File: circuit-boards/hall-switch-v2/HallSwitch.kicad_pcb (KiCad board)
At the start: 2 copper layers, 19.1 x 17.8 mm, 16 parts, among them J1 0705550037, U1 US5881ESE

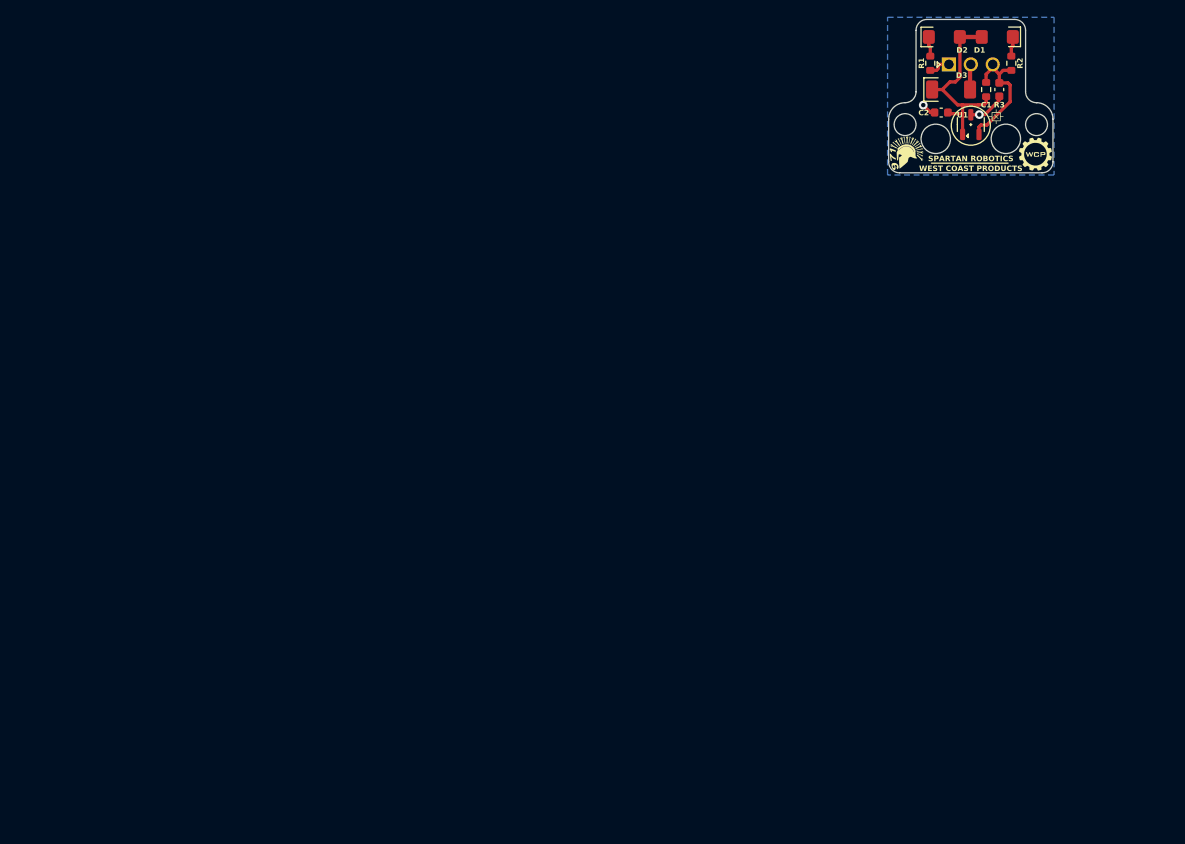
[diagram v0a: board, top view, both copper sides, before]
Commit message: Export files for new pcbs + board characteristics
Signed-off-by: Alex lenkov <Alexander.i.lenkov@gmail.com>
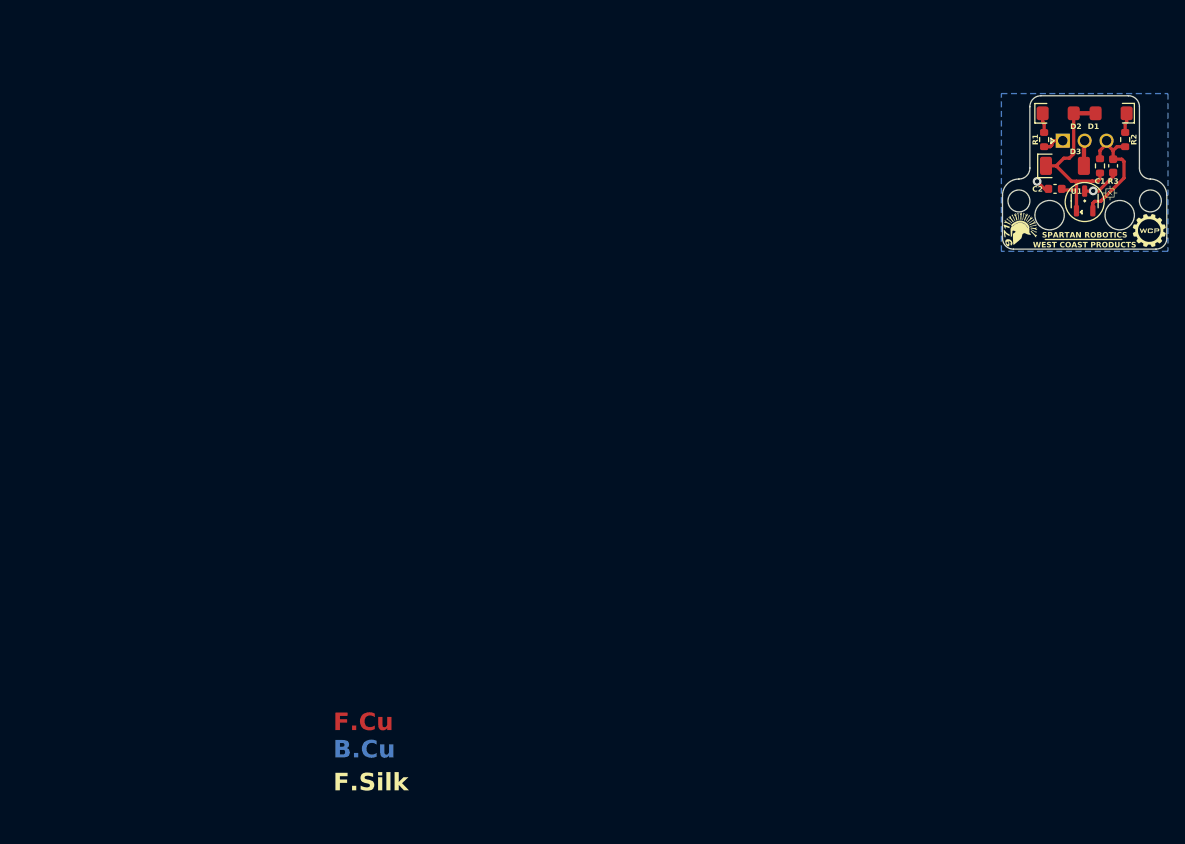
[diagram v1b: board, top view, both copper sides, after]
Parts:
- moved G*** 15.9 mm to (132.6, 115.2)
- moved G*** 15.9 mm to (140.2, 110.4)
- moved R1 15.9 mm to (135.5, 105.0)
- moved D1 15.9 mm to (143.3, 102.0)
- moved D2 15.9 mm to (137.2, 102.0)
- moved G*** 15.9 mm to (143.1, 111.2)
- moved G*** 15.9 mm to (147.7, 115.6)
- moved H1 15.9 mm to (132.6, 112.1)
- moved H2 15.9 mm to (147.8, 112.1)
- moved J1 15.9 mm to (140.2, 109.5)
- moved U1 15.9 mm to (140.2, 112.1)
- moved C1 15.9 mm to (143.5, 108.1)
- moved C2 15.9 mm to (136.8, 110.7)
- moved D3 15.9 mm to (137.9, 108.1)
- moved R2 15.9 mm to (144.9, 105.0)
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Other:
- board text added: "0"
- board text added: "0 mils"
- board text added: "0.0000 mm / 0.2540 mm"
- board text added: "0.02"
- board text added: "0.3000 mm"
- board text added: "0.3937 mils"
- board text added: "1"
- board text added: "1 oz"
- board text added: "1.37795 mils"
- board text added: "1.6000 mm"
- board text added: "1.Layers: 2 2.Thickness: 1.6 3.Surface finish: HASL 4.Outer Copper Weight: 1oz 5.Via covering: Tented 6.Min hole size: .3mm 7.Gold Fingers: No 8.Castellated Holes: No 9.Edge Plating: No"
- board text added: "19.0500 mm x 17.7800 mm"
- board text added: "2"
- board text added: "3.3"
- board text added: "4.5"
- board text added: "59.44882 mils"
- board text added: "B.Cu"
- board text added: "B.Mask"
- board text added: "B.Paste"
- board text added: "B.Silk"
- board text added: "B.Silkscreen"
- board text added: "BOARD CHARACTERISTICS"
- board text added: "Board Thickness:"
- board text added: "Board overall dimensions:"
- board text added: "Bottom Silk Screen"
- board text added: "Bottom Solder Mask"
- board text added: "Bottom Solder Paste"
- board text added: "Castellated pads:"
- board text added: "Color"
- board text added: "Copper Finish:"
- board text added: "Copper Layer Count:"
- board text added: "Dielectric"
- board text added: "Edge card connectors:"
- board text added: "Edge.Cuts"
- board text added: "Epsilon R"
- board text added: "F.Cu"
- board text added: "F.Mask"
- board text added: "F.Paste"
- board text added: "F.Silk"
- board text added: "F.Silkscreen"
- board text added: "FR4"
- board text added: "Impedance Control:"
- board text added: "LAYERS"
- board text added: "Layer Name"
- board text added: "Loss Tangent"
- board text added: "Margin"
- board text added: "Material"
- board text added: "Min hole diameter:"
- board text added: "Min track/spacing:"
- board text added: "NOTES"
- board text added: "No"
- board text added: "None"
- board text added: "Not specified"
- board text added: "Outer Copper Weight:"
- board text added: "Plated Board Edge:"
- board text added: "Tented"
- board text added: "Thickness (mils)"
- board text added: "Top Silk Screen"
- board text added: "Top Solder Mask"
- board text added: "Top Solder Paste"
- board text added: "Type"
- board text added: "Via type:"
- board text added: "copper"
- board text added: "core"

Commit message: Fix pcb fab layers
Signed-off-by: Alex lenkov <Alexander.i.lenkov@gmail.com>
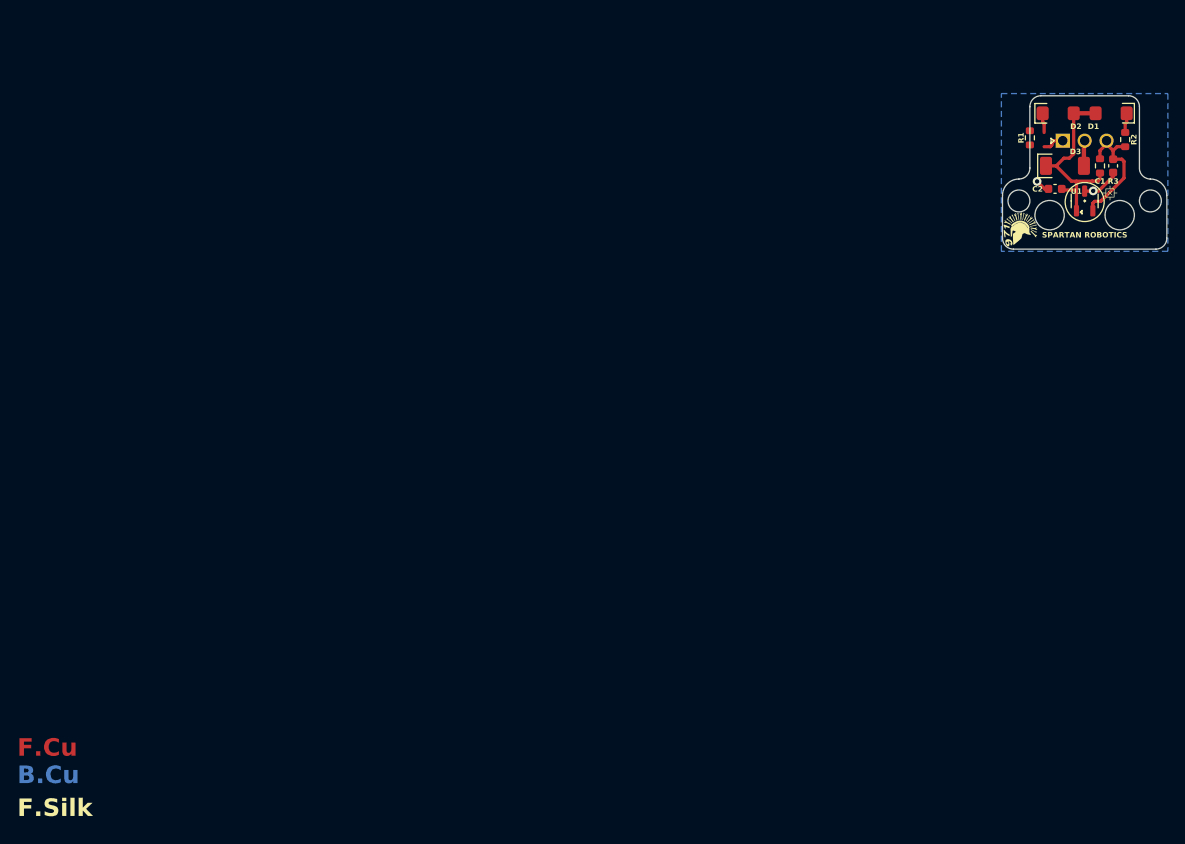
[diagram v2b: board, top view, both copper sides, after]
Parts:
- moved R1 1.66 mm to (133.8, 104.8)
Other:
- board text added: "BACK"
- board text added: "FRONT"
- board text removed: "1 oz"
- board text removed: "Outer Copper Weight:"
- board text removed: "Tented"
- board text removed: "Via type:"

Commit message: Checking in Hall Switch Gerbers
Signed-off-by: Scott Berman <scott.berman@bluerivertech.com>
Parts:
- removed the G*** at (132.6, 115.2)
- moved R1 1.66 mm to (135.5, 105.0)
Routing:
- net GND: track 8.90 -> 11.0 mm
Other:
- board size 19.1 x 17.8 mm -> 19.1 x 18.4 mm
- board text added: "971 SPARTAN ROBOTICS"
- board text added: "GND +5V SIG"
- board text added: "Hall Switch V2"
- board text removed: "+5V"
- board text removed: "GND"
- board text removed: "Hall Switch"
- board text removed: "Rev. 2"
- board text removed: "SPARTAN ROBOTICS"
